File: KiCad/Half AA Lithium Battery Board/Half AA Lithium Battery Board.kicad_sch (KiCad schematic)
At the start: 4 parts, among them J1 Conn_01x04_Pin

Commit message: Update diode
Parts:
- D1: value 1N5817 -> 1N4148; footprint Diode_THT:D_DO-41_SOD81_P7.62mm_Horizontal -> Diode_THT:D_DO-35_SOD27_P7.62mm_Horizontal
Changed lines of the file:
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@@
       (effects (font (size 1.27 1.27)) (justify right))
     )
-    (property "Value" "1N5817" (at 107.95 121.92 90)
+    (property "Value" "1N4148" (at 107.95 121.92 90)
       (effects (font (size 1.27 1.27)) (justify right))
     )
-    (property "Footprint" "Diode_THT:D_DO-41_SOD81_P7.62mm_Horizontal" (at 105.41 120.65 0)
+    (property "Footprint" "Diode_THT:D_DO-35_SOD27_P7.62mm_Horizontal" (at 105.41 120.65 0)
       (effects (font (size 1.27 1.27)) hide)
     )

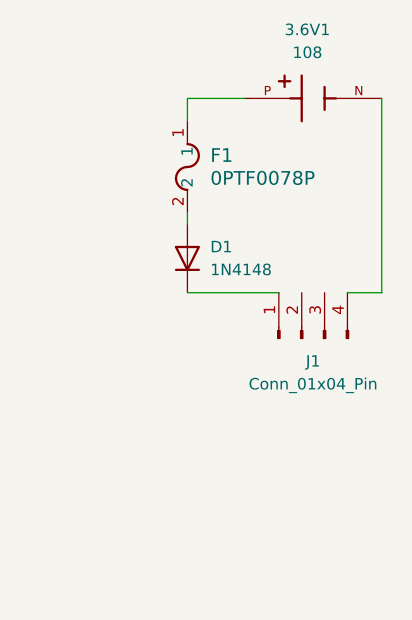
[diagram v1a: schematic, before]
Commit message: add ideal diode
replace traditional diode with ideal diode chip
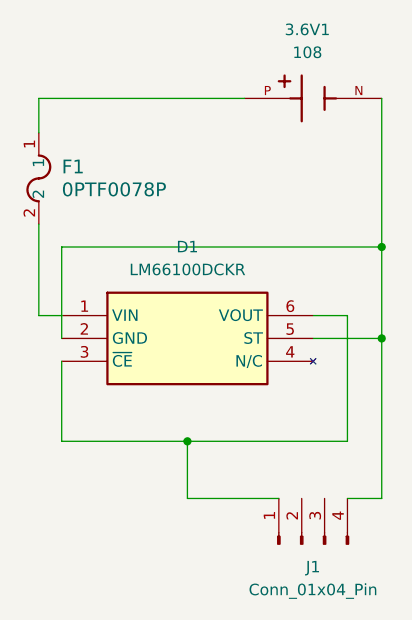
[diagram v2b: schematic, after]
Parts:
- removed D1: 1N4148, Diode_THT:D_DO-35_SOD27_P7.62mm_Horizontal, symbol Device:D
- added D1: LM66100DCKR, SOP65P210X110-6N, symbol LM66100DCKR:LM66100DCKR
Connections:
- net at J1.1 (Pin_1): now also D1.3 (~{CE}), D1.6 (VOUT)
- net at 3.6V1.N, J1.4 (Pin_4): now also D1.2 (GND), D1.5 (ST)
- net at F1.2: now also D1.1 (VIN)
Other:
- moved on the sheet: F1, J1
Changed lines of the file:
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@@
 (kicad_sch (version 20230121) (generator eeschema)
   (paper "A4")
-  (wire (pts (xy 105.41 124.46) (xy 115.57 124.46))
-    (stroke (width 0) (type default))
-  )
-  (wire (pts (xy 105.41 115.57) (xy 105.41 116.84))
-    (stroke (width 0) (type default))
-  )
-  (wire (pts (xy 111.76 102.87) (xy 105.41 102.87))
-    (stroke (width 0) (type default))
-  )
-  (wire (pts (xy 127 124.46) (xy 123.19 124.46))
-    (stroke (width 0) (type default))
-  )
-  (wire (pts (xy 127 102.87) (xy 127 124.46))
-    (stroke (width 0) (type default))
-  )
-  (wire (pts (xy 105.41 102.87) (xy 105.41 105.41))
-    (stroke (width 0) (type default))
-  )
-  (symbol (lib_id "Connector:Conn_01x04_Pin") (at 118.11 129.54 90) (unit 1)
-    (in_bom yes) (on_board yes) (dnp no) (fields_autoplaced)
-    (property "Reference" "J1" (at 119.38 132.08 90)
-      (effects (font (size 1.27 1.27)))
-    )
-    (property "Value" "Conn_01x04_Pin" (at 119.38 134.62 90)
-      (effects (font (size 1.27 1.27)))
-    )
-    (property "Footprint" "Connector_PinHeader_2.54mm:PinHeader_1x04_P2.54mm_Vertical" (at 118.11 129.54 0)
+  (junction (at 127 119.38) (diameter 0) (color 0 0 0 0)
+  )
+  (junction (at 127 129.54) (diameter 0) (color 0 0 0 0)
+  )
+  (junction (at 105.41 140.97) (diameter 0) (color 0 0 0 0)
+  )
+  (wire (pts (xy 91.44 140.97) (xy 105.41 140.97))
+    (stroke (width 0) (type default))
+  )
+  (wire (pts (xy 123.19 140.97) (xy 105.41 140.97))
+    (stroke (width 0) (type default))
+  )
+  (wire (pts (xy 127 119.38) (xy 127 129.54))
+    (stroke (width 0) (type default))
+  )
+  (wire (pts (xy 88.9 116.84) (xy 88.9 127))
+    (stroke (width 0) (type default))
+  )
+  (wire (pts (xy 105.41 147.32) (xy 115.57 147.32))
+    (stroke (width 0) (type default))
+  )
+  (wire (pts (xy 88.9 127) (xy 91.44 127))
+    (stroke (width 0) (type default))
+  )
+  (wire (pts (xy 91.44 132.08) (xy 91.44 140.97))
+    (stroke (width 0) (type default))
+  )
+  (wire (pts (xy 127 129.54) (xy 127 147.32))
+    (stroke (width 0) (type default))
+  )
+  (wire (pts (xy 119.38 127) (xy 123.19 127))
+    (stroke (width 0) (type default))
+  )
+  (wire (pts (xy 91.44 119.38) (xy 127 119.38))
+    (stroke (width 0) (type default))
+  )
+  (wire (pts (xy 111.76 102.87) (xy 88.9 102.87))
+    (stroke (width 0) (type default))
+  )
+  (wire (pts (xy 127 147.32) (xy 123.19 147.32))
+    (stroke (width 0) (type default))
+  )
+  (wire (pts (xy 119.38 129.54) (xy 127 129.54))
+    (stroke (width 0) (type default))
+  )
+  (wire (pts (xy 127 102.87) (xy 127 119.38))
+    (stroke (width 0) (type default))
+  )
+  (wire (pts (xy 123.19 127) (xy 123.19 140.97))
+    (stroke (width 0) (type default))
+  )
+  (wire (pts (xy 105.41 140.97) (xy 105.41 147.32))
+    (stroke (width 0) (type default))
+  )
+  (wire (pts (xy 91.44 119.38) (xy 91.44 129.54))
+    (stroke (width 0) (type default))
+  )
+  (wire (pts (xy 88.9 102.87) (xy 88.9 106.68))
+    (stroke (width 0) (type default))
+  )
+  (symbol (lib_id "Connector:Conn_01x04_Pin") (at 118.11 152.4 90) (unit 1)
+    (in_bom yes) (on_board yes) (dnp no) (fields_autoplaced)
+    (property "Reference" "J1" (at 119.38 154.94 90)
+      (effects (font (size 1.27 1.27)))
+    )
+    (property "Value" "Conn_01x04_Pin" (at 119.38 157.48 90)
+      (effects (font (size 1.27 1.27)))
+    )
+    (property "Footprint" "Connector_PinHeader_2.54mm:PinHeader_1x04_P2.54mm_Vertical" (at 118.11 152.4 0)
       (effects (font (size 1.27 1.27)) hide)
     )
-    (property "Datasheet" "~" (at 118.11 129.54 0)
+    (property "Datasheet" "~" (at 118.11 152.4 0)
       (effects (font (size 1.27 1.27)) hide)
     )
@@
     )
   )
-  (symbol (lib_id "Device:D") (at 105.41 120.65 90) (unit 1)
-    (in_bom yes) (on_board yes) (dnp no) (fields_autoplaced)
-    (property "Reference" "D1" (at 107.95 119.38 90)
-      (effects (font (size 1.27 1.27)) (justify right))
-    )
-    (property "Value" "1N4148" (at 107.95 121.92 90)
-      (effects (font (size 1.27 1.27)) (justify right))
-    )
-    (property "Footprint" "Diode_THT:D_DO-35_SOD27_P7.62mm_Horizontal" (at 105.41 120.65 0)
-      (effects (font (size 1.27 1.27)) hide)
-    )
-    (property "Datasheet" "~" (at 105.41 120.65 0)
-      (effects (font (size 1.27 1.27)) hide)
-    )
-    (property "Sim.Device" "D" (at 105.41 120.65 0)
-      (effects (font (size 1.27 1.27)) hide)
-    )
-    (property "Sim.Pins" "1=K 2=A" (at 105.41 120.65 0)
-      (effects (font (size 1.27 1.27)) hide)
-    )
-    (pin "1")
-    (pin "2")
-    (instances
-      (project "Half AA Lithium Battery Board"
-        (path "/68e6b58b-2241-4e17-911d-3a0f695e834b"
-          (reference "D1") (unit 1)
-        )
-      )
-    )
-  )
   (symbol (lib_id "108:108") (at 119.38 102.87 0) (unit 1)
     (in_bom yes) (on_board yes) (dnp no) (fields_autoplaced)
@@
     )
   )
-  (symbol (lib_id "2023-10-26_08-36-46:0PTF0078P") (at 105.41 105.41 270) (unit 1)
-    (in_bom yes) (on_board yes) (dnp no) (fields_autoplaced)
-    (property "Reference" "F1" (at 107.95 109.22 90)
+  (symbol (lib_id "LM66100DCKR:LM66100DCKR") (at 91.44 127 0) (unit 1)
+    (in_bom yes) (on_board yes) (dnp no) (fields_autoplaced)
+    (property "Reference" "D1" (at 105.41 119.38 0)
+      (effects (font (size 1.27 1.27)))
+    )
+    (property "Value" "LM66100DCKR" (at 105.41 121.92 0)
+      (effects (font (size 1.27 1.27)))
+    )
+    (property "Footprint" "SOP65P210X110-6N" (at 115.57 221.92 0)
+      (effects (font (size 1.27 1.27)) (justify left top) hide)
+    )
+    (property "Datasheet" "http://www.ti.com/lit/gpn/LM66100" (at 115.57 321.92 0)
+      (effects (font (size 1.27 1.27)) (justify left top) hide)
+    )
+    (property "Height" "1.1" (at 115.57 521.92 0)
+      (effects (font (size 1.27 1.27)) (justify left top) hide)
+    )
+    (property "Manufacturer_Name" "Texas Instruments" (at 115.57 621.92 0)
+      (effects (font (size 1.27 1.27)) (justify left top) hide)
+    )
+    (property "Manufacturer_Part_Number" "LM66100DCKR" (at 115.57 721.92 0)
+      (effects (font (size 1.27 1.27)) (justify left top) hide)
+    )
+    (property "Mouser Part Number" "595-LM66100DCKR" (at 115.57 821.92 0)
+      (effects (font (size 1.27 1.27)) (justify left top) hide)
+    )
+    (property "Mouser Price/Stock" "https://www.mouser.co.uk/ProductDetail/Texas-Instruments/LM66100DCKR?qs=vLWxofP3U2y2yPPrXoBBoA%3D%3D" (at 115.57 921.92 0)
+      (effects (font (size 1.27 1.27)) (justify left top) hide)
+    )
+    (property "Arrow Part Number" "LM66100DCKR" (at 115.57 1021.92 0)
+      (effects (font (size 1.27 1.27)) (justify left top) hide)
+    )
+    (property "Arrow Price/Stock" "https://www.arrow.com/en/products/lm66100dckr/texas-instruments?region=nac" (at 115.57 1121.92 0)
+      (effects (font (size 1.27 1.27)) (justify left top) hide)
+    )
+    (pin "1")
+    (pin "2")
+    (pin "3")
+    (pin "4")
+    (pin "5")
+    (pin "6")
+    (instances
+      (project "Half AA Lithium Battery Board"
+        (path "/68e6b58b-2241-4e17-911d-3a0f695e834b"
+          (reference "D1") (unit 1)
+        )
+      )
+    )
+  )
+  (symbol (lib_id "2023-10-26_08-36-46:0PTF0078P") (at 88.9 106.68 270) (unit 1)
+    (in_bom yes) (on_board yes) (dnp no) (fields_autoplaced)
+    (property "Reference" "F1" (at 91.44 110.49 90)
       (effects (font (size 1.524 1.524)) (justify left))
     )
-    (property "Value" "0PTF0078P" (at 107.95 111.76 90)
+    (property "Value" "0PTF0078P" (at 91.44 113.03 90)
       (effects (font (size 1.524 1.524)) (justify left))
     )
-    (property "Footprint" "FUSE_0PTF0078P_LTF" (at 105.41 105.41 0)
+    (property "Footprint" "FUSE_0PTF0078P_LTF" (at 88.9 106.68 0)
       (effects (font (size 1.27 1.27) italic) hide)
     )
-    (property "Datasheet" "0PTF0078P" (at 105.41 105.41 0)
+    (property "Datasheet" "0PTF0078P" (at 88.9 106.68 0)
       (effects (font (size 1.27 1.27) italic) hide)
     )
